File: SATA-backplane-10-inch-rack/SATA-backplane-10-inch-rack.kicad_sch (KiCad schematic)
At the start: 15 parts, among them J101 Conn_01x06, Q101 DMG1012UW, Q102 DMG1012UW

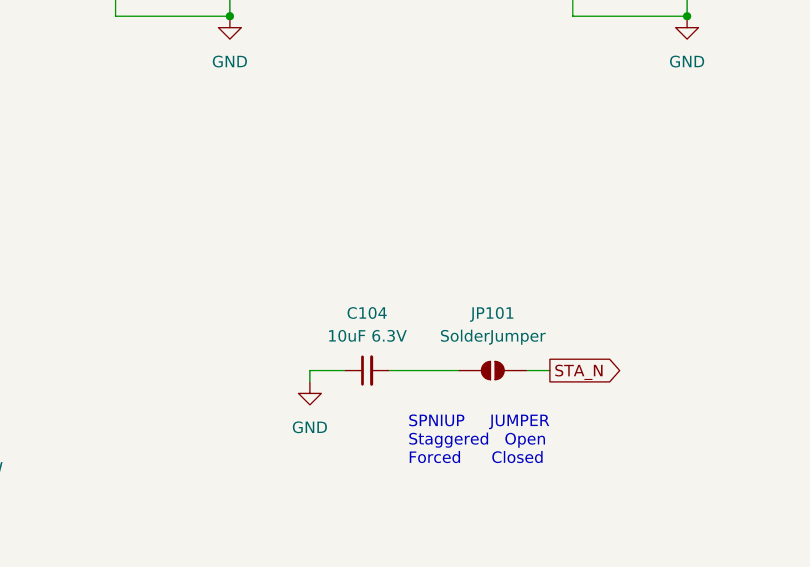
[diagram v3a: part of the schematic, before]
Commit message: add capacitor discharge
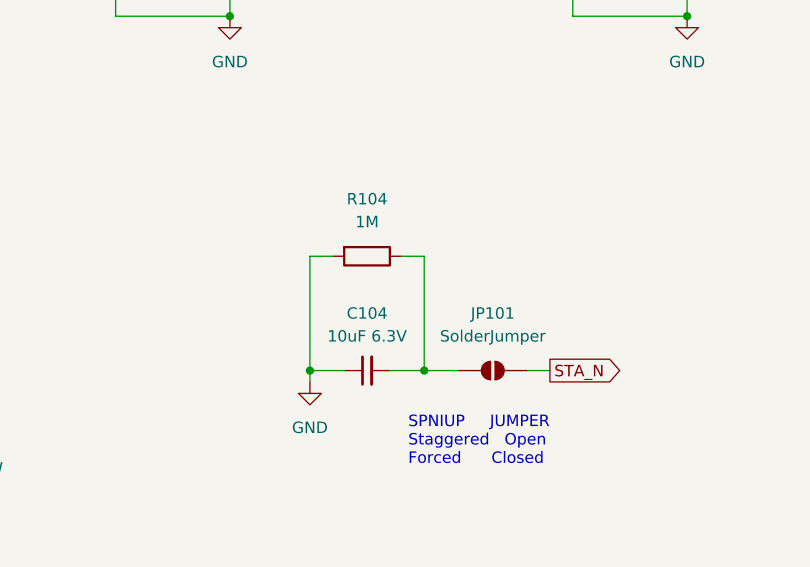
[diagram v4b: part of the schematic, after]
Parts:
- added R104: 1M, Resistor_SMD:R_0805_2012Metric_Pad1.20x1.40mm_HandSolder, symbol Device:R
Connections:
- net GND: now also R104.2
- net at C104.2, JP101.1 (A): now also R104.1
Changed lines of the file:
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@@
 (kicad_sch
-	(version 20231120)
+	(version 20250114)
 	(generator "eeschema")
-	(generator_version "8.0")
+	(generator_version "9.0")
 	(paper "A4")
+	(text "SPNIUP     JUMPER\nStaggered   Open\nForced      Closed"
+		(exclude_from_sim no)
+		(at 151.892 98.044 0)
+		(effects
+			(font
+				(size 1.27 1.27)
+			)
+			(justify left)
+		)
+	)
+	(junction
+		(at 140.97 90.17)
+		(diameter 0)
+		(color 0 0 0 0)
+	)
 	(junction
 		(at 68.58 99.06)
@@
 	)
 	(junction
+		(at 153.67 90.17)
+		(diameter 0)
+		(color 0 0 0 0)
+	)
+	(junction
 		(at 182.88 38.1)
 		(diameter 0)
@@
 	(wire
 		(pts
+			(xy 143.51 77.47) (xy 140.97 77.47)
+		)
+		(stroke
+			(width 0)
+			(type default)
+		)
+	)
+	(wire
+		(pts
 			(xy 220.98 46.99) (xy 220.98 50.8)
 		)
@@
 	(wire
 		(pts
+			(xy 151.13 77.47) (xy 153.67 77.47)
+		)
+		(stroke
+			(width 0)
+			(type default)
+		)
+	)
+	(wire
+		(pts
 			(xy 220.98 38.1) (xy 233.68 38.1)
 		)
@@
 	(wire
 		(pts
+			(xy 153.67 90.17) (xy 157.48 90.17)
+		)
+		(stroke
+			(width 0)
+			(type default)
+		)
+	)
+	(wire
+		(pts
 			(xy 140.97 90.17) (xy 144.78 90.17)
 		)
@@
 	(wire
 		(pts
+			(xy 153.67 77.47) (xy 153.67 90.17)
+		)
+		(stroke
+			(width 0)
+			(type default)
+		)
+	)
+	(wire
+		(pts
 			(xy 220.98 50.8) (xy 233.68 50.8)
 		)
@@
 	(wire
 		(pts
-			(xy 170.18 46.99) (xy 170.18 50.8)
+			(xy 140.97 77.47) (xy 140.97 90.17)
 		)
 		(stroke
@@
 	(wire
 		(pts
-			(xy 149.86 90.17) (xy 157.48 90.17)
+			(xy 170.18 46.99) (xy 170.18 50.8)
 		)
 		(stroke
@@
 	(wire
 		(pts
-			(xy 132.08 38.1) (xy 132.08 40.64)
+			(xy 149.86 90.17) (xy 153.67 90.17)
 		)
 		(stroke
@@
 		)
 	)
-	(text "SPNIUP     JUMPER\nStaggered   Open\nForced      Closed"
-		(exclude_from_sim no)
-		(at 151.892 98.044 0)
-		(effects
-			(font
-				(size 1.27 1.27)
-			)
-			(justify left)
+	(wire
+		(pts
+			(xy 132.08 38.1) (xy 132.08 40.64)
+		)
+		(stroke
+			(width 0)
+			(type default)
 		)
 	)
 	(label "+5V"
 		(at 170.18 38.1 0)
-		(fields_autoplaced yes)
 		(effects
 			(font
@@
 	(label "GND"
 		(at 91.44 45.72 180)
-		(fields_autoplaced yes)
 		(effects
 			(font
@@
 	(label "+12V"
 		(at 91.44 38.1 180)
-		(fields_autoplaced yes)
 		(effects
 			(font
@@
 	(label "GND"
 		(at 91.44 40.64 180)
-		(fields_autoplaced yes)
 		(effects
 			(font
@@
 	(label "GND"
 		(at 91.44 35.56 180)
-		(fields_autoplaced yes)
 		(effects
 			(font
@@
 	(label "+3.3V"
 		(at 220.98 38.1 0)
-		(fields_autoplaced yes)
 		(effects
 			(font
@@
 	(label "+3.3V"
 		(at 91.44 48.26 180)
-		(fields_autoplaced yes)
 		(effects
 			(font
@@
 	(label "+12V"
 		(at 119.38 38.1 0)
-		(fields_autoplaced yes)
 		(effects
 			(font
@@
 	(label "+5V"
 		(at 91.44 43.18 180)
-		(fields_autoplaced yes)
 		(effects
 			(font
@@
 		(at 161.29 90.17 0)
 		(unit 1)
-		(exclude_from_sim yes)
+		(exclude_from_sim no)
 		(in_bom no)
 		(on_board yes)
@@
 	)
 	(symbol
+		(lib_id "Device:R")
+		(at 147.32 77.47 270)
+		(unit 1)
+		(exclude_from_sim no)
+		(in_bom yes)
+		(on_board yes)
+		(dnp no)
+		(fields_autoplaced yes)
+		(property "Reference" "R104"
+			(at 147.32 71.12 90)
+			(effects
+				(font
+					(size 1.27 1.27)
+				)
+			)
+		)
+		(property "Value" "1M"
+			(at 147.32 73.66 90)
+			(effects
+				(font
+					(size 1.27 1.27)
+				)
+			)
+		)
+		(property "Footprint" "Resistor_SMD:R_0805_2012Metric_Pad1.20x1.40mm_HandSolder"
+			(at 147.32 75.692 90)
+			(effects
+				(font
+					(size 1.27 1.27)
+				)
+				(hide yes)
+			)
+		)
+		(property "Datasheet" "~"
+			(at 147.32 77.47 0)
+			(effects
+				(font
+					(size 1.27 1.27)
+				)
+				(hide yes)
+			)
+		)
+		(property "Description" "Resistor"
+			(at 147.32 77.47 0)
+			(effects
+				(font
+					(size 1.27 1.27)
+				)
+				(hide yes)
+			)
+		)
+		(pin "1"
+		)
+		(pin "2"
+		)
+		(instances
+			(project "SATA-backplane-10-inch-rack"
+				(path "/c1a10ee3-1b0d-4235-ba02-c6ac86e8d48c"
+					(reference "R104")
+					(unit 1)
+				)
+			)
+		)
+	)
+	(symbol
 		(lib_id "power:GND")
 		(at 132.08 50.8 0)
@@
 		(at 185.42 132.08)
 		(size 8.89 21.59)
+		(exclude_from_sim no)
+		(in_bom yes)
+		(on_board yes)
+		(dnp no)
 		(fields_autoplaced yes)
 		(stroke
@@
 		(at 160.02 132.08)
 		(size 8.89 21.59)
+		(exclude_from_sim no)
+		(in_bom yes)
+		(on_board yes)
+		(dnp no)
 		(fields_autoplaced yes)
 		(stroke
@@
 		(at 96.52 132.08)
 		(size 8.89 21.59)
+		(exclude_from_sim no)
+		(in_bom yes)
+		(on_board yes)
+		(dnp no)
 		(fields_autoplaced yes)
 		(stroke
@@
 		(at 210.82 132.08)
 		(size 8.89 21.59)
+		(exclude_from_sim no)
+		(in_bom yes)
+		(on_board yes)
+		(dnp no)
 		(fields_autoplaced yes)
 		(stroke
@@
 		(at 172.72 132.08)
 		(size 8.89 21.59)
+		(exclude_from_sim no)
+		(in_bom yes)
+		(on_board yes)
+		(dnp no)
 		(fields_autoplaced yes)
 		(stroke
@@
 		(at 198.12 132.08)
 		(size 8.89 21.59)
+		(exclude_from_sim no)
+		(in_bom yes)
+		(on_board yes)
+		(dnp no)
 		(fields_autoplaced yes)
 		(stroke
@@
 		(at 83.82 132.08)
 		(size 8.89 21.59)
+		(exclude_from_sim no)
+		(in_bom yes)
+		(on_board yes)
+		(dnp no)
 		(fields_autoplaced yes)
 		(stroke
@@
 		(at 147.32 132.08)
 		(size 8.89 21.59)
+		(exclude_from_sim no)
+		(in_bom yes)
+		(on_board yes)
+		(dnp no)
 		(fields_autoplaced yes)
 		(stroke
@@
 		(at 109.22 132.08)
 		(size 8.89 21.59)
+		(exclude_from_sim no)
+		(in_bom yes)
+		(on_board yes)
+		(dnp no)
 		(fields_autoplaced yes)
 		(stroke
@@
 		(at 121.92 132.08)
 		(size 8.89 21.59)
+		(exclude_from_sim no)
+		(in_bom yes)
+		(on_board yes)
+		(dnp no)
 		(fields_autoplaced yes)
 		(stroke
@@
 		(at 223.52 132.08)
 		(size 8.89 21.59)
+		(exclude_from_sim no)
+		(in_bom yes)
+		(on_board yes)
+		(dnp no)
 		(fields_autoplaced yes)
 		(stroke
@@
 		(at 134.62 132.08)
 		(size 8.89 21.59)
+		(exclude_from_sim no)
+		(in_bom yes)
+		(on_board yes)
+		(dnp no)
 		(fields_autoplaced yes)
 		(stroke
@@
 		)
 	)
+	(embedded_fonts no)
 )

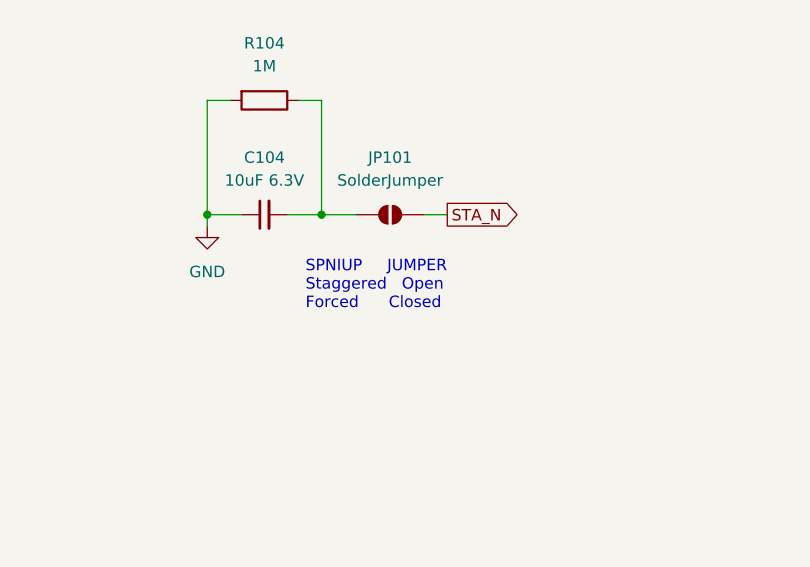
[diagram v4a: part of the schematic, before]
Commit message: Add 6 x 3½" HDD outline and measures
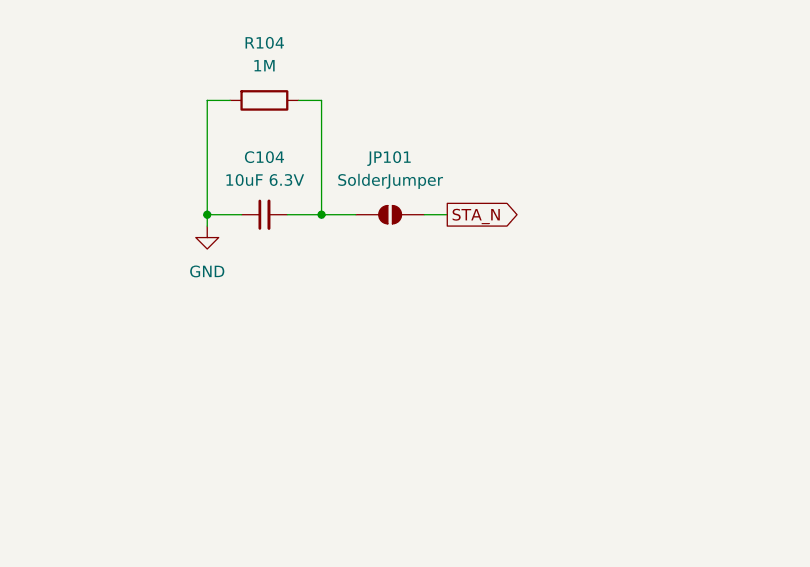
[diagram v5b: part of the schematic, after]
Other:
- note removed: "SPNIUP JUMPER Staggered Open Forced Closed"
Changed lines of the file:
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@@
 	(generator_version "9.0")
 	(paper "A4")
-	(text "SPNIUP     JUMPER\nStaggered   Open\nForced      Closed"
-		(exclude_from_sim no)
-		(at 151.892 98.044 0)
-		(effects
-			(font
-				(size 1.27 1.27)
-			)
-			(justify left)
-		)
-	)
 	(junction
 		(at 140.97 90.17)
@@
 		)
 	)
+	(table
+		(column_count 2)
+		(border
+			(external yes)
+			(header yes)
+			(stroke
+				(width 0)
+				(type solid)
+			)
+		)
+		(separators
+			(rows no)
+			(cols no)
+		)
+		(column_widths 15.24 10.16)
+		(row_heights 3.81 2.54 3.81)
+		(cells
+			(table_cell "SPINUP mode"
+				(exclude_from_sim no)
+				(at 151.13 93.98 0)
+				(size 15.24 3.81)
+				(margins 0.9525 0.9525 0.9525 0.9525)
+				(span 1 1)
+				(fill
+					(type color)
+					(color 218 239 255 1)
+				)
+				(effects
+					(font
+						(size 1.27 1.27)
+						(thickness 0.254)
+						(bold yes)
+					)
+					(justify left top)
+				)
+			)
+			(table_cell "JP101"
+				(exclude_from_sim no)
+				(at 166.37 93.98 0)
+				(size 10.16 3.81)
+				(margins 0.9525 0.9525 0.9525 0.9525)
+				(span 1 1)
+				(fill
+					(type color)
+					(color 218 239 255 1)
+				)
+				(effects
+					(font
+						(size 1.27 1.27)
+						(thickness 0.254)
+						(bold yes)
+					)
+					(justify left top)
+				)
+			)
+			(table_cell "Staggered"
+				(exclude_from_sim no)
+				(at 151.13 97.79 0)
+				(size 15.24 2.54)
+				(margins 0.9525 0.9525 0.9525 0.9525)
+				(span 1 1)
+				(fill
+					(type none)
+				)
+				(effects
+					(font
+						(size 1.27 1.27)
+					)
+					(justify left top)
+				)
+			)
+			(table_cell "OPEN"
+				(exclude_from_sim no)
+				(at 166.37 97.79 0)
+				(size 10.16 2.54)
+				(margins 0.9525 0.9525 0.9525 0.9525)
+				(span 1 1)
+				(fill
+					(type none)
+				)
+				(effects
+					(font
+						(size 1.27 1.27)
+					)
+					(justify left top)
+				)
+			)
+			(table_cell "Forced"
+				(exclude_from_sim no)
+				(at 151.13 100.33 0)
+				(size 15.24 3.81)
+				(margins 0.9525 0.9525 0.9525 0.9525)
+				(span 1 1)
+				(fill
+					(type none)
+				)
+				(effects
+					(font
+						(size 1.27 1.27)
+					)
+					(justify left top)
+				)
+			)
+			(table_cell "CLOSED"
+				(exclude_from_sim no)
+				(at 166.37 100.33 0)
+				(size 10.16 3.81)
+				(margins 0.9525 0.9525 0.9525 0.9525)
+				(span 1 1)
+				(fill
+					(type none)
+				)
+				(effects
+					(font
+						(size 1.27 1.27)
+					)
+					(justify left top)
+				)
+			)
+		)
+	)

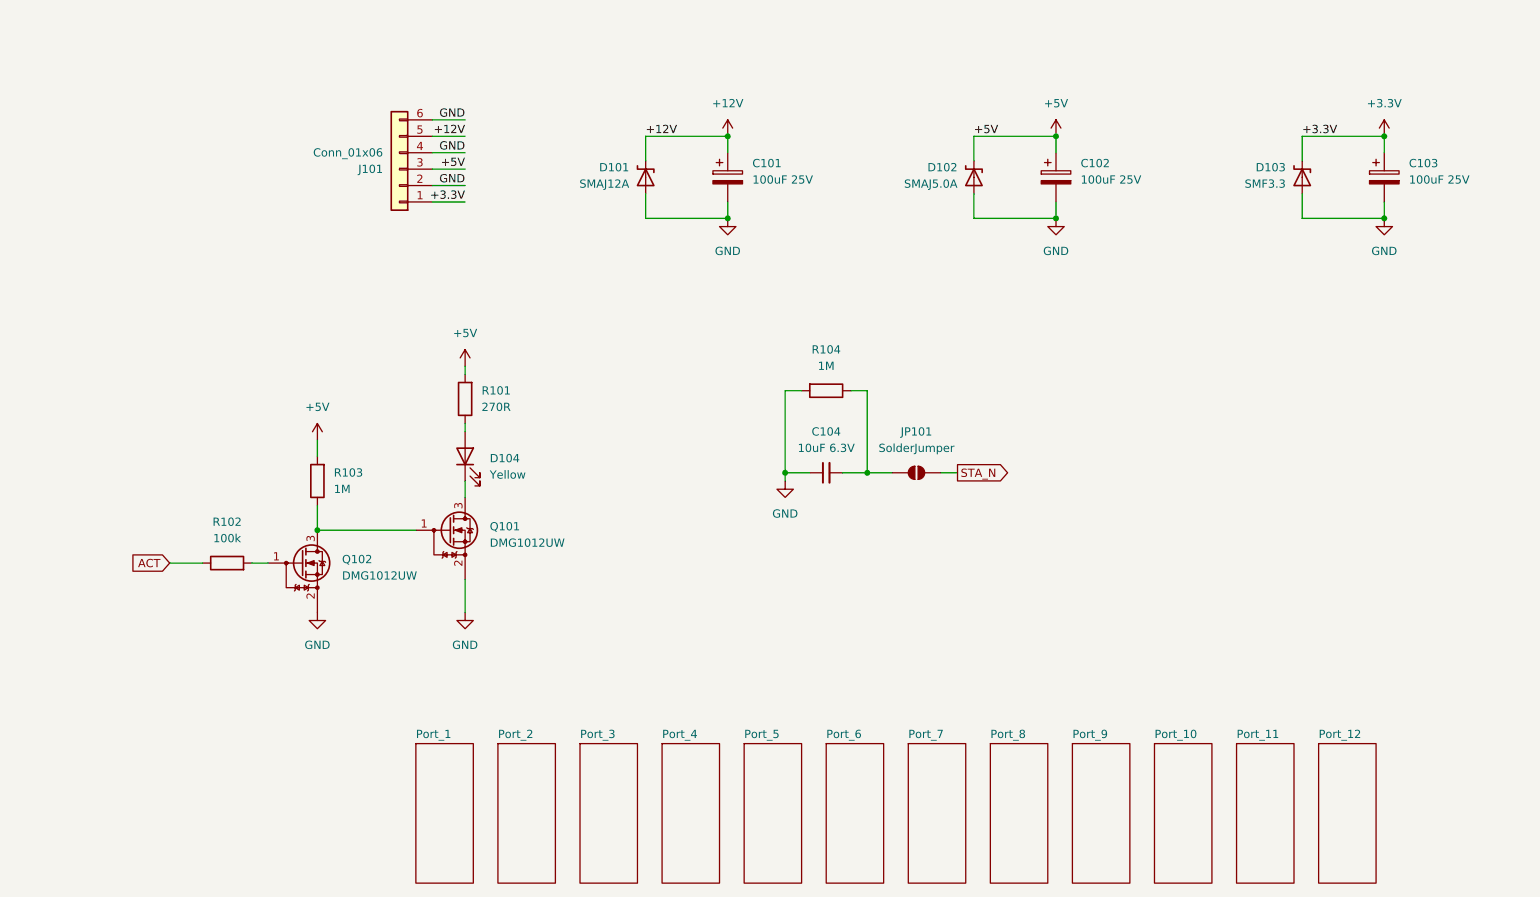
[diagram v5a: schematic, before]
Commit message: Adapt to 6 x 3½" version using the multichannel tool
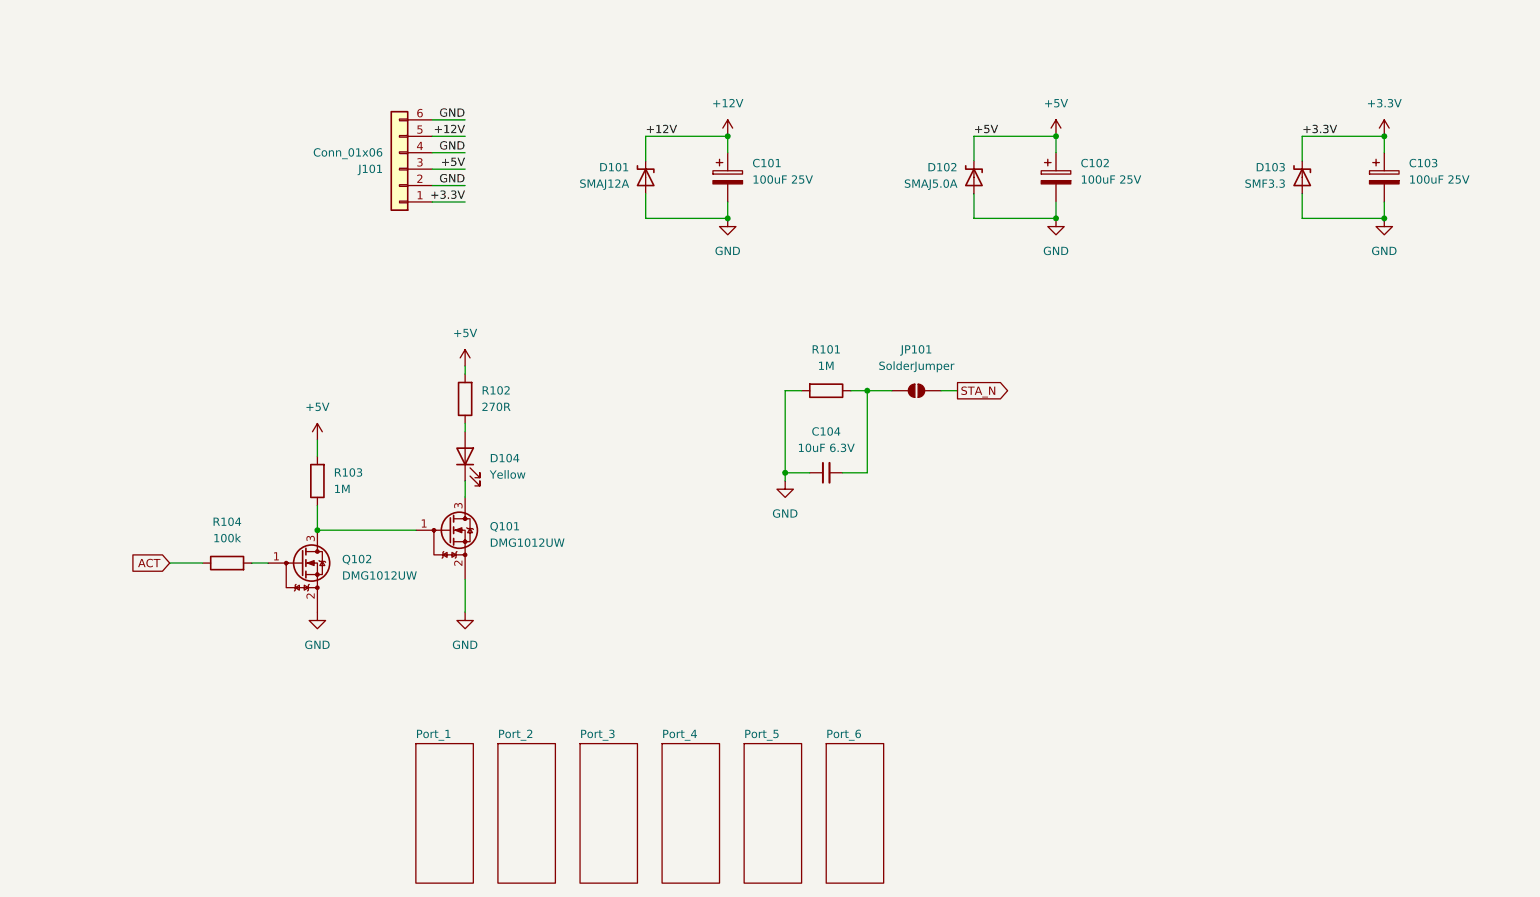
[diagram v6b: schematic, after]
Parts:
- renumbered R104 to R101, R101 to R102, R102 to R104
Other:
- removed sheet Port_10
- removed sheet Port_11
- removed sheet Port_12
- removed sheet Port_7
- removed sheet Port_8
- removed sheet Port_9
- moved on the sheet: JP101

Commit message: Fix Sta/Act signal definition
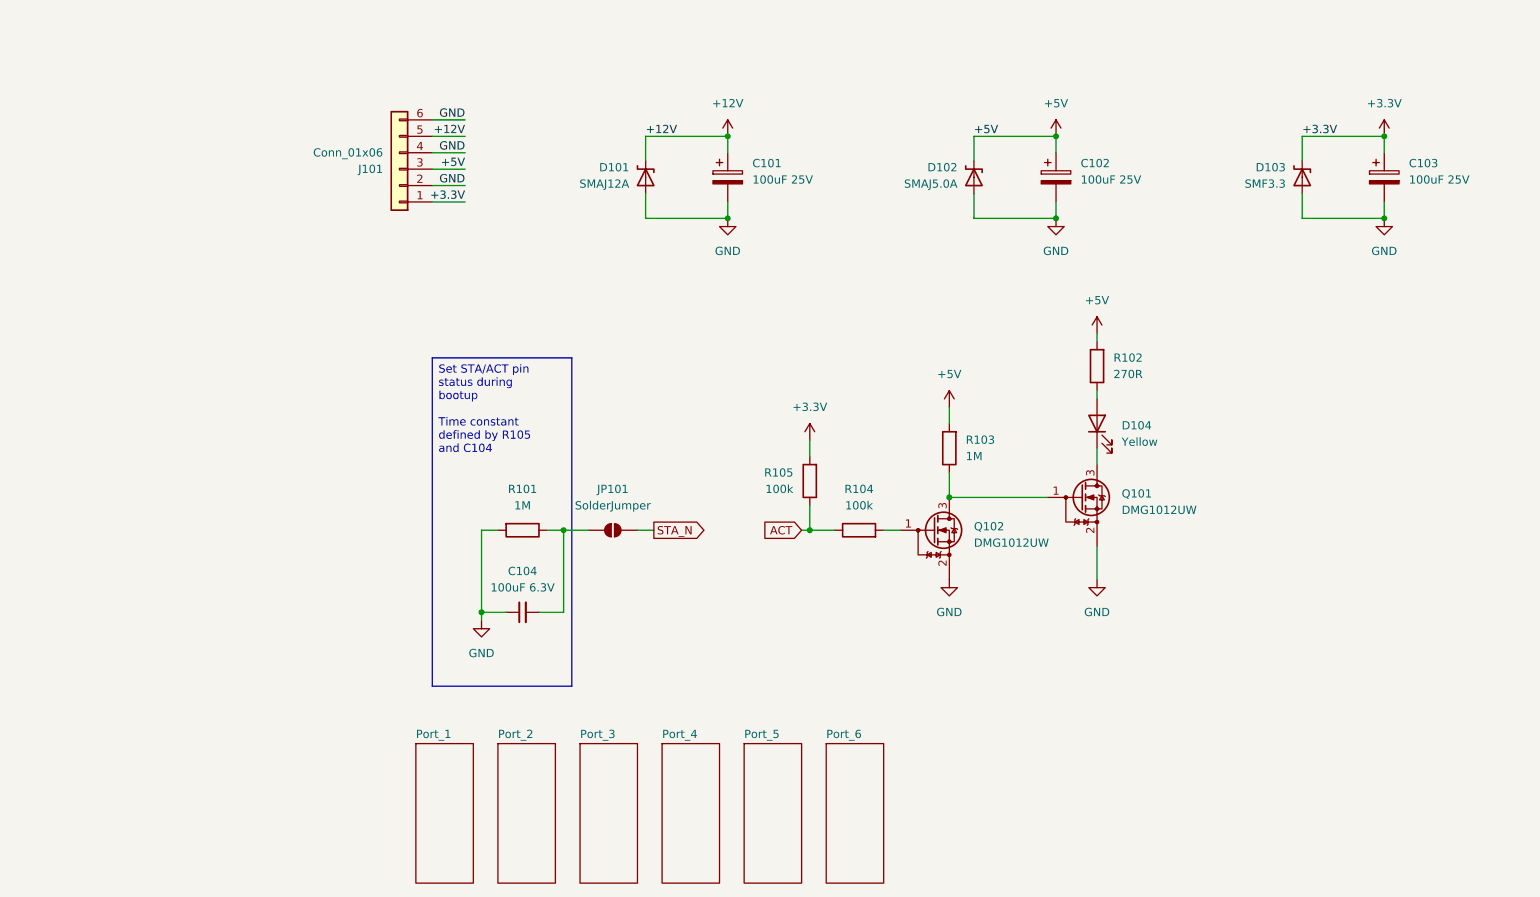
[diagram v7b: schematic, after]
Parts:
- added R105: 100k, Resistor_SMD:R_0805_2012Metric_Pad1.20x1.40mm_HandSolder, symbol Device:R
- C104: value 10uF 6.3V -> 100uF 6.3V; footprint Capacitor_SMD:C_0805_2012Metric_Pad1.18x1.45mm_HandSolder -> Capacitor_SMD:C_1210_3225Metric_Pad1.33x2.70mm_HandSolder
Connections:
- net +3.3V: now also R105.2
- net ACT: now also R105.1
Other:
- moved on the sheet: C104, D104, JP101, Q101, Q102, R101, R102, R103, R104
